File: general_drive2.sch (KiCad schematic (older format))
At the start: 9 parts, among them P20 CONN_1, P21 CONN_1, Q7 PIP-3104

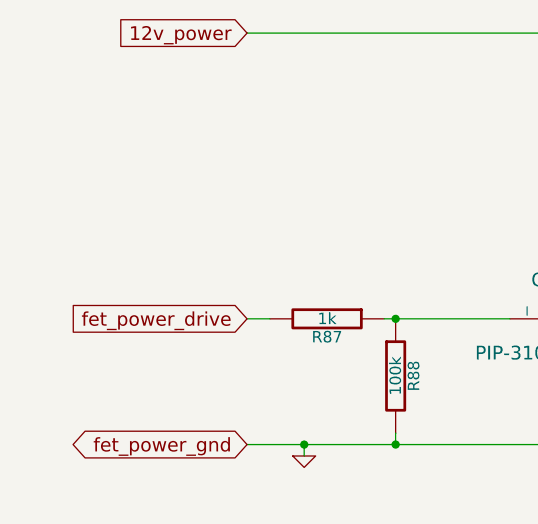
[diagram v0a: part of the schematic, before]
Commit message: Removed LM1815 options. Now adaptive mode and square waves are the default,
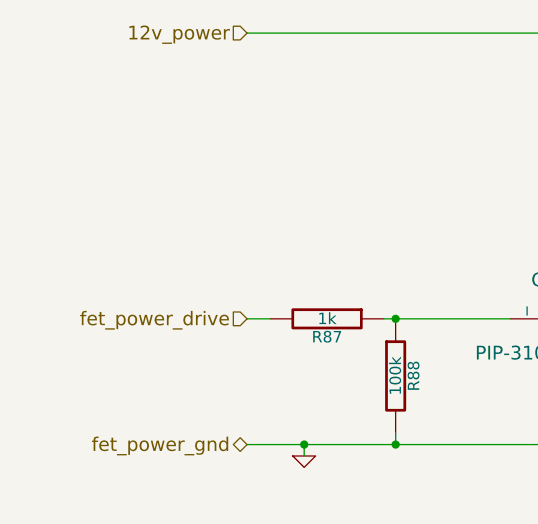
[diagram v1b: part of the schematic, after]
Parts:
- C45: Field1 (none) -> newark,97k4148; Field2 (none) -> vendor1, smd w hem; Field3 (none) -> vendor2, thru w hem; Field4 (none) -> vendor2, smd w hem; Field5 (none) -> 200,V; Field6 (none) -> 10,%; Field7 (none) -> multilayer ceramic; Field8 (none) -> other,more,stuff
- D71: Field1 (none) -> newark,58k2469; Field2 (none) -> vendor1, smd w hem; Field3 (none) -> vendor2, thru w hem; Field4 (none) -> vendor2, smd w hem; Field5 (none) -> x,x; Field6 (none) -> x,x; Field7 (none) -> green; Field8 (none) -> other,more,stuff
- Q7: Field1 (none) -> digi,PIP3104-ND; Field2 (none) -> vendor1, smd w hem; Field3 (none) -> vendor2, thru w hem; Field4 (none) -> vendor2, smd w hem; Field5 (none) -> 8,A; Field6 (none) -> x,x; Field7 (none) -> TOPFET; Field8 (none) -> other,more,stuff
- R87: Field1 (none) -> newark,38k0327; Field2 (none) -> vendor1, smd w hem; Field3 (none) -> vendor2, thru w hem; Field4 (none) -> vendor2, smd w hem; Field5 (none) -> 250,mW; Field6 (none) -> 5,%; Field7 (none) -> carbon film; Field8 (none) -> other,more,stuff
- R88: Field1 (none) -> newark,38k0329; Field2 (none) -> vendor1, smd w hem; Field3 (none) -> vendor2, thru w hem; Field4 (none) -> vendor2, smd w hem; Field5 (none) -> 250,mW; Field6 (none) -> 5,%; Field7 (none) -> carbon film; Field8 (none) -> other,more,stuff
- R89: Field1 (none) -> newark,38k0340; Field2 (none) -> vendor1, smd w hem; Field3 (none) -> vendor2, thru w hem; Field4 (none) -> vendor2, smd w hem; Field5 (none) -> 1/4,W; Field6 (none) -> 5,%; Field7 (none) -> carbon film; Field8 (none) -> other,more,stuff
- R90: Field1 (none) -> newark,38k0352; Field2 (none) -> vendor1, smd w hem; Field3 (none) -> vendor2, thru w hem; Field4 (none) -> vendor2, smd w hem; Field5 (none) -> 250,mW; Field6 (none) -> 5,%; Field7 (none) -> carbon film; Field8 (none) -> other,more,stuff

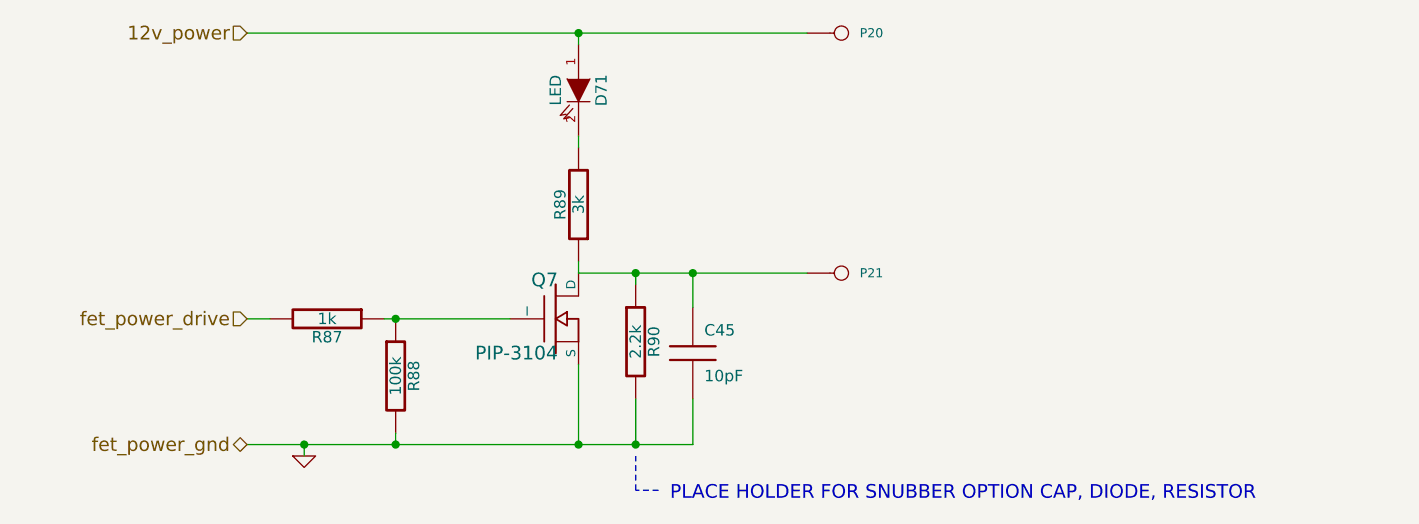
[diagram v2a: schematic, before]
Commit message: Implemented P&H, removed current sense circuitry, removed all unnecessary files from the repo
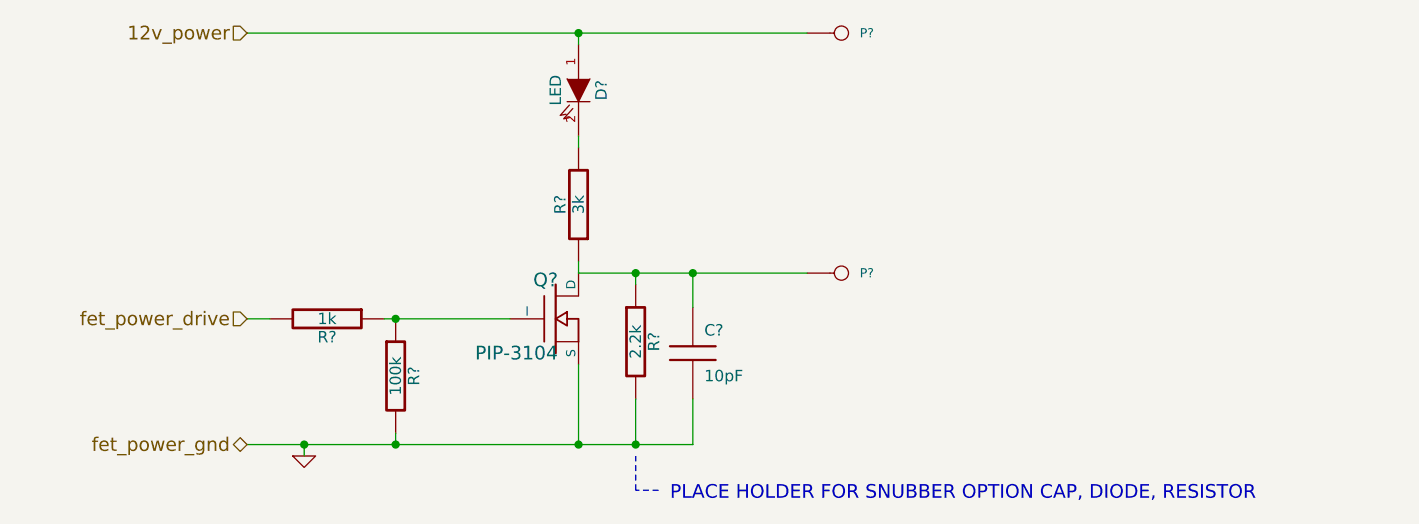
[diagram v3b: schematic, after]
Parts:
- renumbered C45 to C?, D71 to D?, P20 to P?, P21 to P?, Q7 to Q?, R87 to R?, R90 to R?, R88 to R?, R89 to R?
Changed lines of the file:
@@
-EESchema Schematic File Version 2  date Fri 02 Jul 2010 05:44:26 PM ART
+EESchema Schematic File Version 2  date Sat 03 Jul 2010 10:49:02 AM ART
 LIBS:power
 LIBS:freeEMS_lib
@@
 EELAYER END
 $Descr A4 11700 8267
-Sheet 25 41
+Sheet 1 41
 Title "freeEMS 1.0"
-Date "2 jul 2010"
-Rev "A.20"
+Date "3 jul 2010"
+Rev "A.07"
 Comp "diyefi.org"
 Comment1 "general_drive.sch"
@@
 	2250 2300 2350 2300
 Wire Wire Line
-	2850 2300 3400 2300
+	3400 2300 2850 2300
 Wire Wire Line
 	4200 2850 4200 2650
@@
 Connection ~ 3950 2100
 Wire Wire Line
-	2250 1050 4700 1050
+	4700 1050 2250 1050
 Wire Wire Line
 	3700 1500 3700 1550
 Connection ~ 2900 2300
 Wire Wire Line
-	2900 2850 2900 2800
+	2900 2800 2900 2850
 Connection ~ 2900 2850
 $Comp
-L PIP-3104 Q7
+L PIP-3104 Q?
 U 1 1 48B16ED5
 P 3600 2300
-F 0 "Q7" H 3610 2470 60  0000 R CNN
+F 0 "Q?" H 3610 2470 60  0000 R CNN
 F 1 "PIP-3104" H 3610 2150 60  0000 R CNN
 F 2 "TO220_sm" V 3530 3050 60  0001 C CNN
@@
 $EndComp
 $Comp
-L R R89
+L R R?
 U 1 1 48AA2408
 P 3700 1800
-F 0 "R89" V 3780 1800 50  0000 C CNN
+F 0 "R?" V 3780 1800 50  0000 C CNN
 F 1 "3k" V 3700 1800 50  0000 C CNN
 F 2 "R4-SM0805" V 2480 1650 60  0001 C CNN
@@
 $EndComp
 $Comp
-L LED D71
+L LED D?
 U 1 1 48AA23E4
 P 3700 1300
-F 0 "D71" H 3700 1400 50  0000 C CNN
+F 0 "D?" H 3700 1400 50  0000 C CNN
 F 1 "LED" H 3700 1200 50  0000 C CNN
 F 2 "LEDV" V 1380 5250 60  0001 C CNN
@@
 $EndComp
 $Comp
-L CONN_1 P21
+L CONN_1 P?
 U 1 1 48AA1A18
 P 4850 2100
-F 0 "P21" H 4930 2100 40  0000 L CNN
+F 0 "P?" H 4930 2100 40  0000 L CNN
 F 1 "CONN_1" H 4850 2155 30  0001 C CNN
 F 2 "1PIN" V 1130 3400 60  0001 C CNN
@@
 $EndComp
 $Comp
-L CONN_1 P20
+L CONN_1 P?
 U 1 1 48AA1A13
 P 4850 1050
-F 0 "P20" H 4930 1050 40  0000 L CNN
+F 0 "P?" H 4930 1050 40  0000 L CNN
 F 1 "CONN_1" H 4850 1105 30  0001 C CNN
 F 2 "1PIN" V 1130 2550 60  0001 C CNN
@@
 $EndComp
 $Comp
-L R R88
+L R R?
 U 1 1 488C9E4A
 P 2900 2550
-F 0 "R88" V 2980 2550 50  0000 C CNN
+F 0 "R?" V 2980 2550 50  0000 C CNN
 F 1 "100k" V 2900 2550 50  0000 C CNN
 F 2 "R4-SM0805" V 3080 2650 60  0001 C CNN
@@
 $EndComp
 $Comp
-L GND #PWR042
+L GND #PWR?
 U 1 1 488C8987
 P 2500 2900
-F 0 "#PWR042" H 2500 2900 30  0001 C CNN
+F 0 "#PWR?" H 2500 2900 30  0001 C CNN
 F 1 "GND" H 2500 2830 30  0001 C CNN
 	1    2500 2900
@@
 $EndComp
 $Comp
-L C C45
+L C C?
 U 1 1 488A2BA8
 P 4200 2450
-F 0 "C45" H 4250 2550 50  0000 L CNN
+F 0 "C?" H 4250 2550 50  0000 L CNN
 F 1 "10pF" H 4250 2350 50  0000 L CNN
 F 2 "C1V7" V 1130 3400 60  0001 C CNN
@@
 $EndComp
 $Comp
-L R R90
+L R R?
 U 1 1 488A2B90
 P 3950 2400
-F 0 "R90" V 4030 2400 50  0000 C CNN
+F 0 "R?" V 4030 2400 50  0000 C CNN
 F 1 "2.2k" V 3950 2400 50  0000 C CNN
 F 2 "R4-SM0805" V 4130 2500 60  0001 C CNN
@@
 $EndComp
 $Comp
-L R R87
+L R R?
 U 1 1 488A2B3B
 P 2600 2300
-F 0 "R87" V 2680 2300 50  0000 C CNN
+F 0 "R?" V 2680 2300 50  0000 C CNN
 F 1 "1k" V 2600 2300 50  0000 C CNN
 F 2 "R4-SM0805" V 2780 2400 60  0001 C CNN

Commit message: Corrected ERC errors by fixing the custom FreeEMS components pinouts
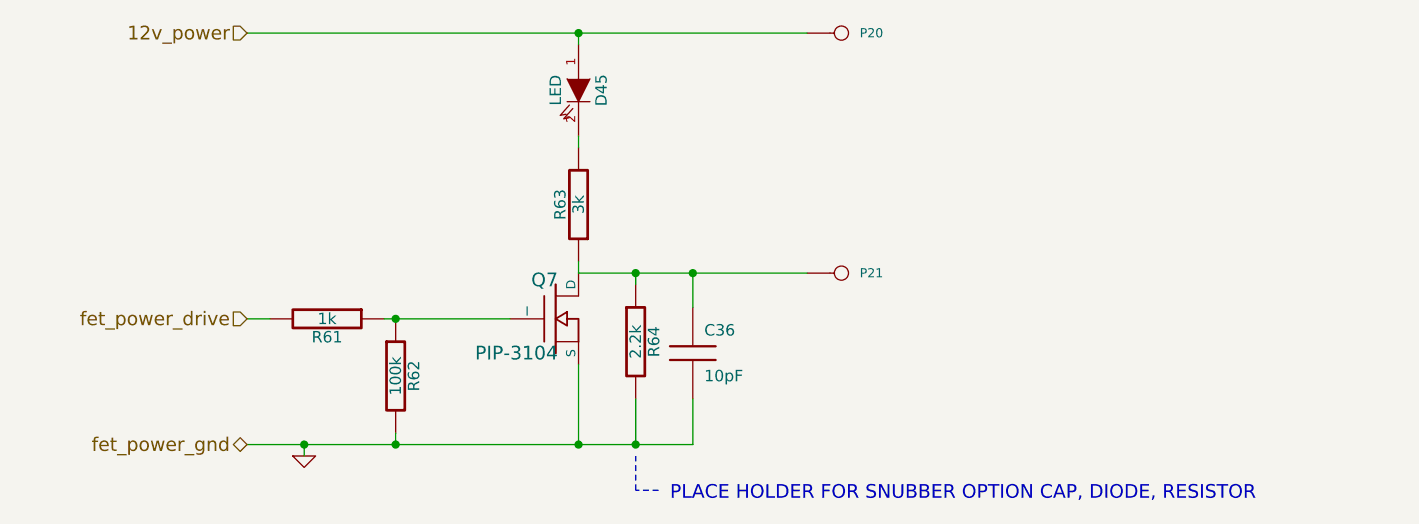
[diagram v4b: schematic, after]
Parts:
- removed C?: 10pF, C1V7, symbol C
- removed D?: LED, LEDV, symbol LED
- removed P? (x2): CONN_1, 1PIN, symbol CONN_1
- removed R?: 2.2k, R4-SM0805, symbol R
- removed R?: 100k, R4-SM0805, symbol R
- removed R?: 3k, R4-SM0805, symbol R
- added C36: 10pF, C1V7, symbol C
- added D45: LED, LEDV, symbol LED
- added P20, P21: CONN_1, 1PIN, symbol CONN_1
- added R62: 100k, R4-SM0805, symbol R
- added R63: 3k, R4-SM0805, symbol R
- added R64: 2.2k, R4-SM0805, symbol R
- gave numbers to parts that had none: 2
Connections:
- net 12v_power: now also D45.1 (A), P20.1
- net GND: now also C36.2, R62.2, R64.2
- net at Q7.1 (I), R61.1: now also R62.1
- net at Q7.2 (D): now also C36.1, P21.1, R63.1, R64.1
- new net: D45.2 (K), R63.2
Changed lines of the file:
@@
-EESchema Schematic File Version 2  date Sat 03 Jul 2010 10:49:02 AM ART
+EESchema Schematic File Version 2  date Sat 03 Jul 2010 12:32:24 PM ART
 LIBS:power
 LIBS:freeEMS_lib
@@
 Connection ~ 2900 2850
 $Comp
-L PIP-3104 Q?
+L PIP-3104 Q7
 U 1 1 48B16ED5
 P 3600 2300
-F 0 "Q?" H 3610 2470 60  0000 R CNN
+F 0 "Q7" H 3610 2470 60  0000 R CNN
 F 1 "PIP-3104" H 3610 2150 60  0000 R CNN
 F 2 "TO220_sm" V 3530 3050 60  0001 C CNN
@@
 $EndComp
 $Comp
-L R R?
-U 1 1 48AA2408
+L R R63
+U 1 1 4C2F5319
 P 3700 1800
-F 0 "R?" V 3780 1800 50  0000 C CNN
+F 0 "R63" V 3780 1800 50  0000 C CNN
 F 1 "3k" V 3700 1800 50  0000 C CNN
 F 2 "R4-SM0805" V 2480 1650 60  0001 C CNN
@@
 $EndComp
 $Comp
-L LED D?
-U 1 1 48AA23E4
+L LED D45
+U 1 1 4C2F5318
 P 3700 1300
-F 0 "D?" H 3700 1400 50  0000 C CNN
+F 0 "D45" H 3700 1400 50  0000 C CNN
 F 1 "LED" H 3700 1200 50  0000 C CNN
 F 2 "LEDV" V 1380 5250 60  0001 C CNN
@@
 $EndComp
 $Comp
-L CONN_1 P?
-U 1 1 48AA1A18
+L CONN_1 P21
+U 1 1 4C2F530D
 P 4850 2100
-F 0 "P?" H 4930 2100 40  0000 L CNN
+F 0 "P21" H 4930 2100 40  0000 L CNN
 F 1 "CONN_1" H 4850 2155 30  0001 C CNN
 F 2 "1PIN" V 1130 3400 60  0001 C CNN
@@
 $EndComp
 $Comp
-L CONN_1 P?
-U 1 1 48AA1A13
+L CONN_1 P20
+U 1 1 4C2F530C
 P 4850 1050
-F 0 "P?" H 4930 1050 40  0000 L CNN
+F 0 "P20" H 4930 1050 40  0000 L CNN
 F 1 "CONN_1" H 4850 1105 30  0001 C CNN
 F 2 "1PIN" V 1130 2550 60  0001 C CNN
@@
 $EndComp
 $Comp
-L R R?
-U 1 1 488C9E4A
+L R R62
+U 1 1 4C2F52DB
 P 2900 2550
-F 0 "R?" V 2980 2550 50  0000 C CNN
+F 0 "R62" V 2980 2550 50  0000 C CNN
 F 1 "100k" V 2900 2550 50  0000 C CNN
 F 2 "R4-SM0805" V 3080 2650 60  0001 C CNN
@@
 $EndComp
 $Comp
-L GND #PWR?
-U 1 1 488C8987
+L GND #PWR063
+U 1 1 4C2F52D8
 P 2500 2900
-F 0 "#PWR?" H 2500 2900 30  0001 C CNN
+F 0 "#PWR063" H 2500 2900 30  0001 C CNN
 F 1 "GND" H 2500 2830 30  0001 C CNN
 	1    2500 2900
@@
 $EndComp
 $Comp
-L C C?
-U 1 1 488A2BA8
+L C C36
+U 1 1 4C2F52D6
 P 4200 2450
-F 0 "C?" H 4250 2550 50  0000 L CNN
+F 0 "C36" H 4250 2550 50  0000 L CNN
 F 1 "10pF" H 4250 2350 50  0000 L CNN
 F 2 "C1V7" V 1130 3400 60  0001 C CNN
@@
 $EndComp
 $Comp
-L R R?
-U 1 1 488A2B90
+L R R64
+U 1 1 4C2F52D5
 P 3950 2400
-F 0 "R?" V 4030 2400 50  0000 C CNN
+F 0 "R64" V 4030 2400 50  0000 C CNN
 F 1 "2.2k" V 3950 2400 50  0000 C CNN
 F 2 "R4-SM0805" V 4130 2500 60  0001 C CNN
@@
 $EndComp
 $Comp
-L R R?
+L R R61
 U 1 1 488A2B3B
 P 2600 2300
-F 0 "R?" V 2680 2300 50  0000 C CNN
+F 0 "R61" V 2680 2300 50  0000 C CNN
 F 1 "1k" V 2600 2300 50  0000 C CNN
 F 2 "R4-SM0805" V 2780 2400 60  0001 C CNN
